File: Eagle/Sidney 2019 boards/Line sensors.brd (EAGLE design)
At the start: 58.2 x 24.2 mm, 19 parts

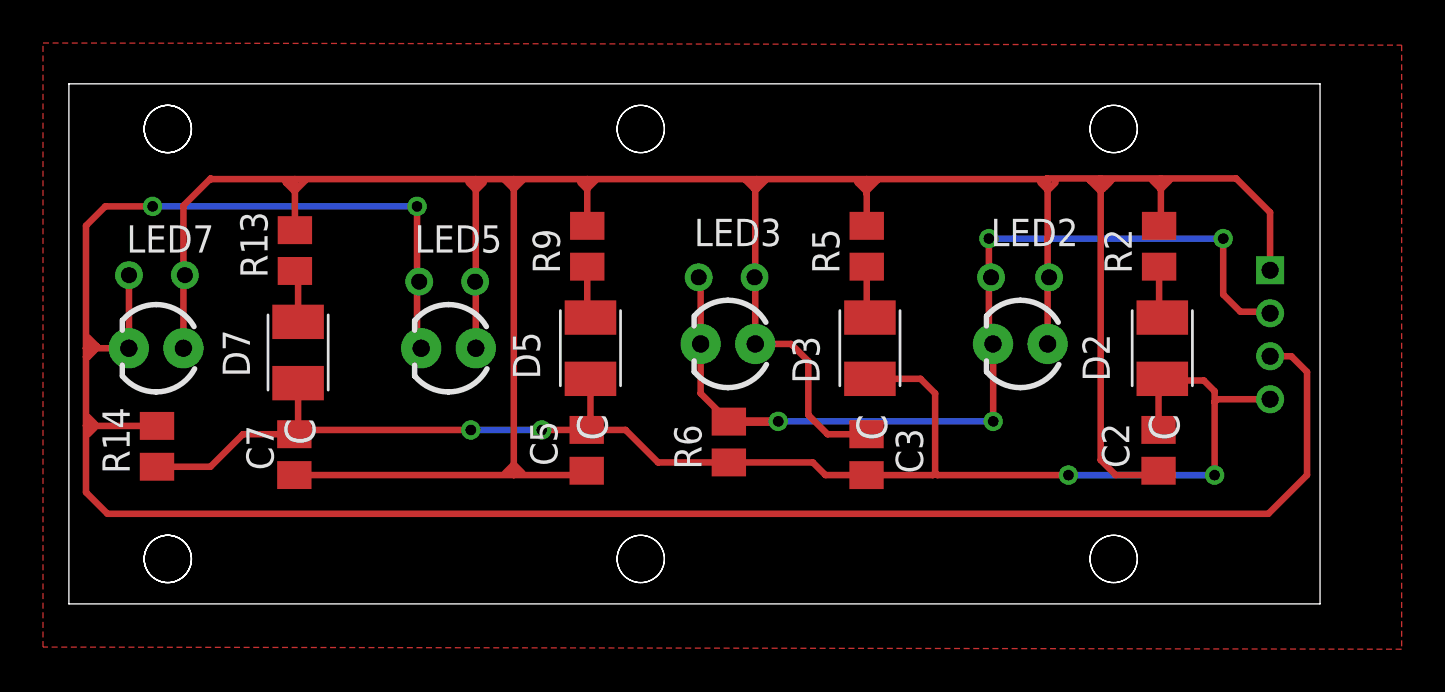
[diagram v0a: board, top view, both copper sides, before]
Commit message: Almost completed components lists
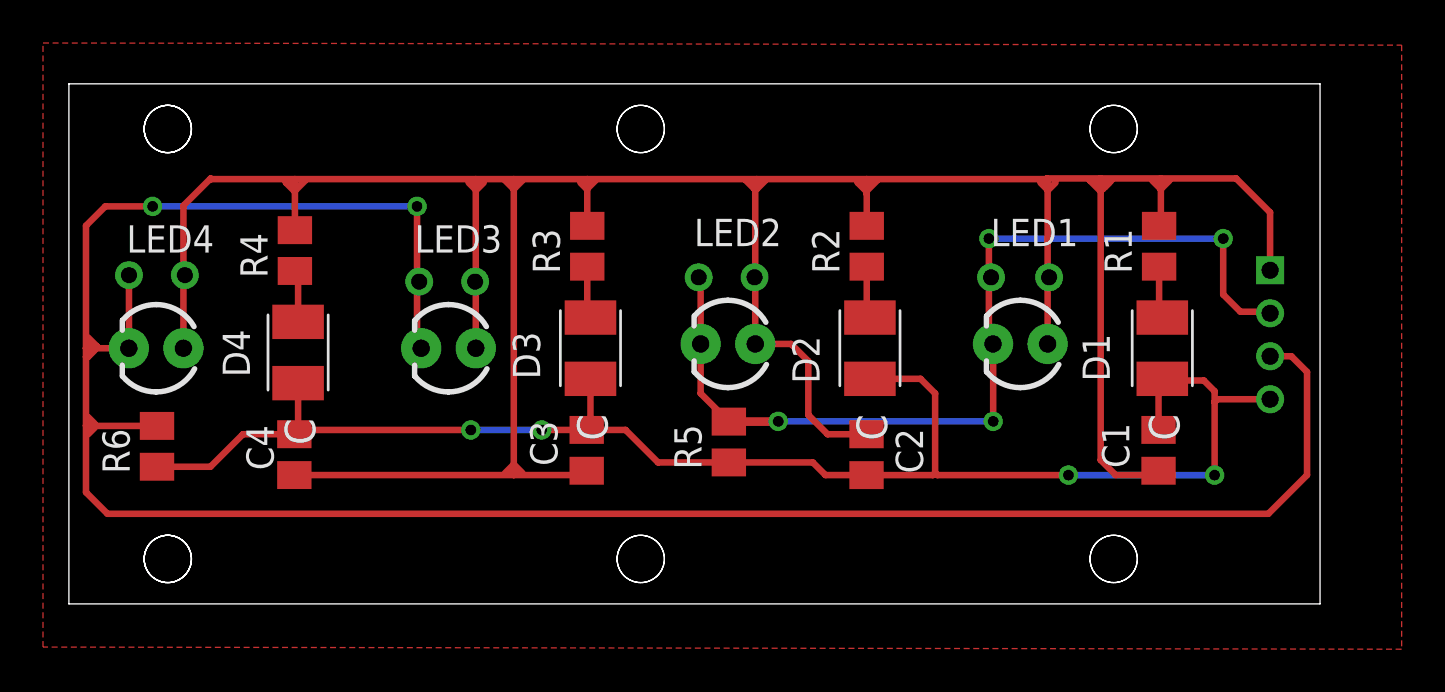
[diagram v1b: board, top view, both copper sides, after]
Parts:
- removed C5: 100n, resistor:M0805
- removed D5: (no value), Wurth_Elektronik_Optoelectronics_rev15b:3528-2PIN
- removed LED5: (no value), SparkFun:LED3MM
- removed R14: 10k, resistor:M0805
- added C1: 100n, resistor:M0805
- added D1: (no value), Wurth_Elektronik_Optoelectronics_rev15b:3528-2PIN
- added LED1: (no value), SparkFun:LED3MM
- added R1: 330, resistor:M0805
- R5: value 330 -> 10k
- moved R6 26.6 mm to (-89.6, -4.76)
- moved D2 13.6 mm to (-56.4, -0.20)
- moved R2 13.6 mm to (-56.6, 4.54)
- moved LED2 13.6 mm to (-63.0, 0.00)
- moved C2 13.6 mm to (-56.6, -5.15), turned to 90 degrees
- moved C3 13.0 mm to (-69.6, -4.95), turned to 270 degrees
- moved LED3 13.0 mm to (-76.0, -0.20)
- moved D3 13.0 mm to (-69.4, -0.20)
- moved R5 11.1 mm to (-63.0, -4.56)
- renumbered C7 to C4, D7 to D4, LED7 to LED4, R13 to R4, R9 to R3
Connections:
- removed net N$4 (its old number): D3.2, R5.1
- new net N$3: D1.2, R1.1
- net 5V: now also C1.2, LED1.A, R1.2; no longer C5.2, LED5.A, R5.2
- net GND: now also C1.1, D1.1, R5.1; no longer C5.1, D5.1, R14.1
- net N$13: now also D3.2; no longer D5.2
- net SIG1: now also LED1.K, R5.2; no longer LED3.K, R6.2
- net SIG2: now also LED3.K, R6.2; no longer LED5.K, R14.2
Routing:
- net N$4 (its old number): track 2.43 -> 0.00 mm
- net N$3: track 0.00 -> 2.43 mm
